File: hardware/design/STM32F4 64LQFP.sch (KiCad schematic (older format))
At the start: 17 parts, among them U1 STM32F40X_LQFP64, X2 8MHz 10ppm

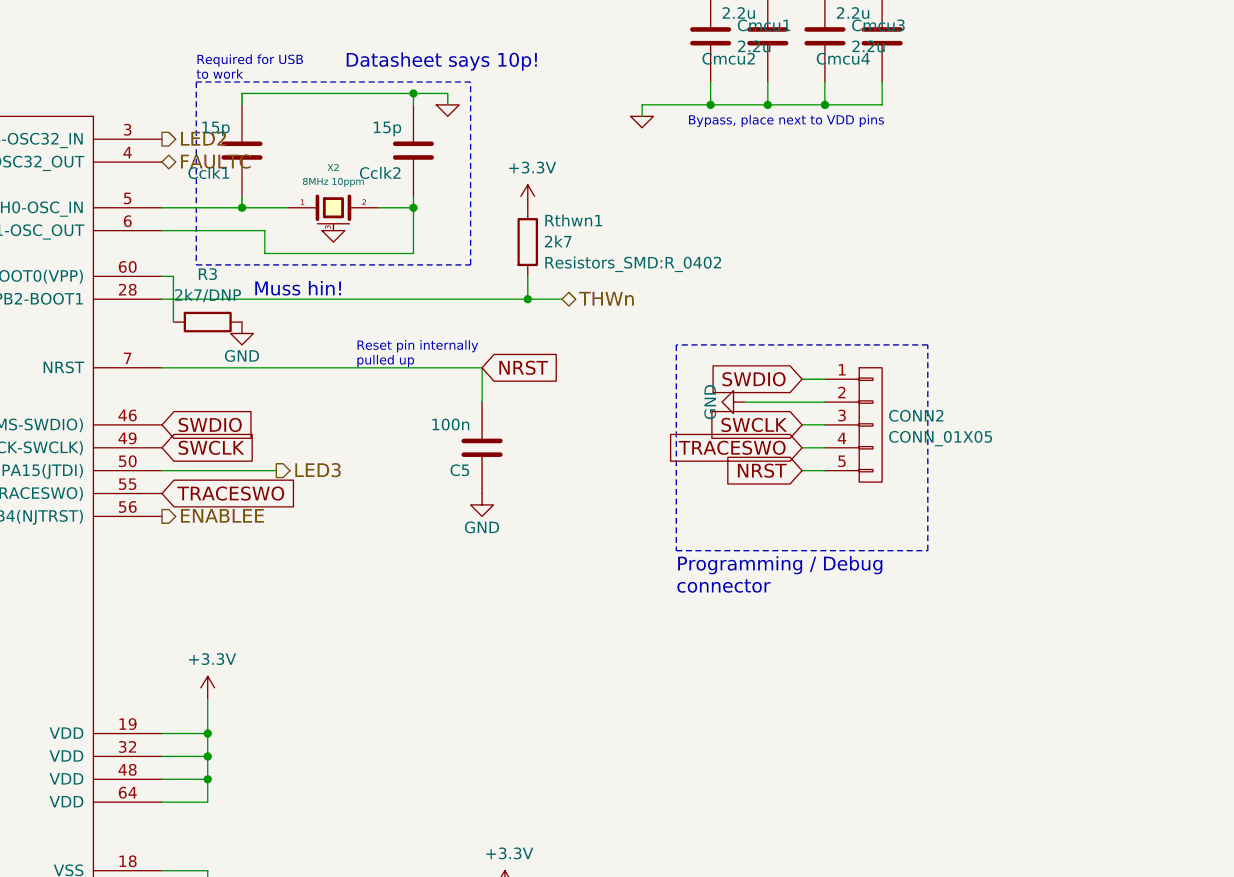
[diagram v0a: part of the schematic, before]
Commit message: Added pads for emergency bootloader execution.
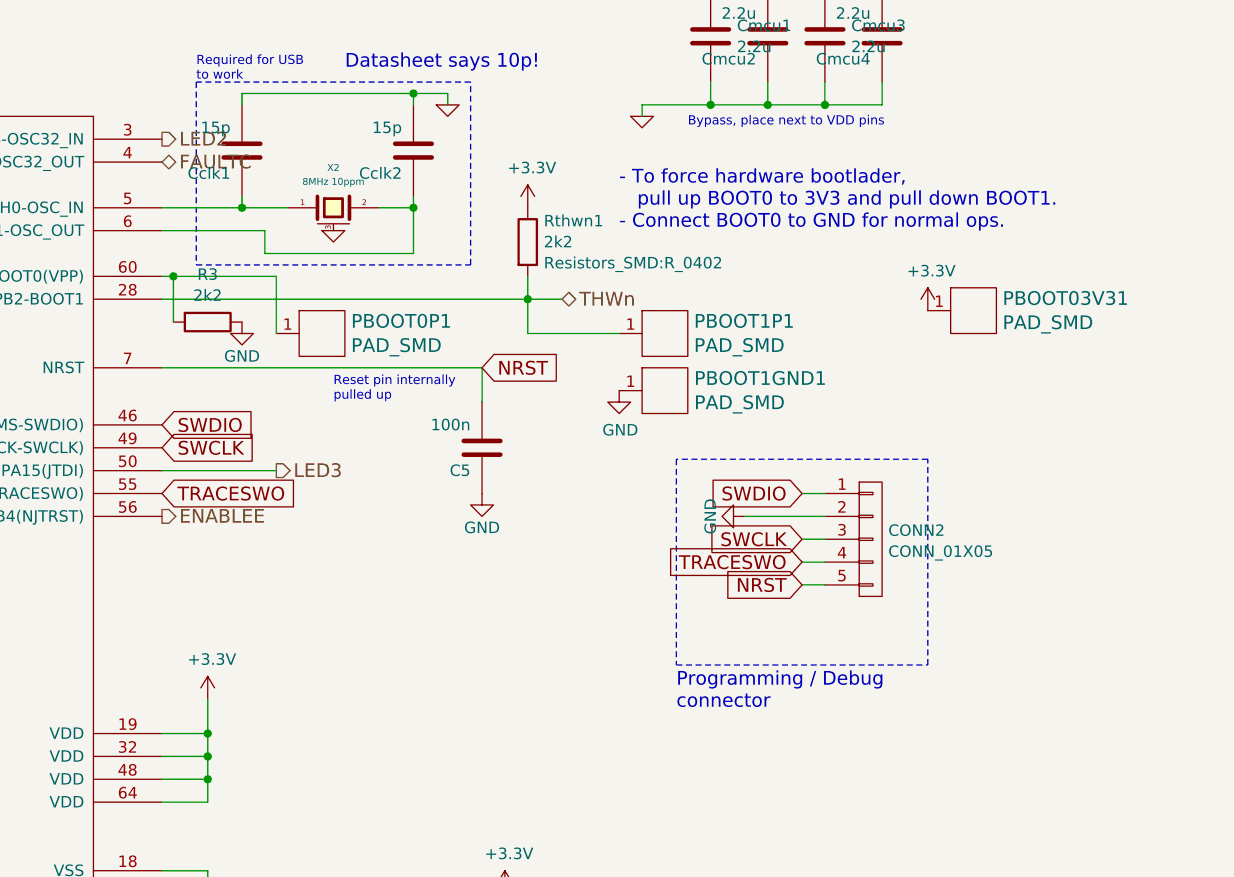
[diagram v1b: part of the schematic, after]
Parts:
- added PBOOT03V31, PBOOT0P1, PBOOT1GND1, PBOOT1P1: PAD_SMD, Pads:PAD_SMD_1x1, symbol PAD_SMD
- R3: value 2k7/DNP -> 2k2
- Rthwn1: value 2k7 -> 2k2
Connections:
- net +3V3: now also PBOOT03V31.1 (PAD)
- net GND: now also PBOOT1GND1.1 (PAD)
- net THWn: now also PBOOT1P1.1 (PAD)
- net at R3.2, U1.60 (BOOT0(VPP)): now also PBOOT0P1.1 (PAD)
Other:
- note added: "- To force hardware bootlader,\n pull up BOOT0 to 3V3 and pull down BOOT1.\n- Connect BOOT0 to GND for normal ops."
- note removed: "Muss hin!"
- moved on the sheet: CONN2
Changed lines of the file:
@@
 	-1   0    0    1
 $EndComp
-Text GLabel 9800 3000 0    60   Input ~ 0
+Text GLabel 9800 3500 0    60   Input ~ 0
 SWCLK
-Text GLabel 9800 2800 0    60   Input ~ 0
+Text GLabel 9800 3300 0    60   Input ~ 0
 SWDIO
-Text GLabel 9800 3200 0    60   Input ~ 0
+Text GLabel 9800 3700 0    60   Input ~ 0
 NRST
 $Comp
@@
 AN_IN
 Wire Notes Line
-	9250 2650 9250 3550
+	9250 3150 9250 4050
 Wire Notes Line
-	9250 3550 10350 3550
+	9250 4050 10350 4050
 Wire Notes Line
-	10350 3550 10350 2650
+	10350 4050 10350 3150
 Wire Notes Line
-	10350 2650 9250 2650
-Text Notes 9250 3750 0    60   ~ 0
+	10350 3150 9250 3150
+Text Notes 9250 4250 0    60   ~ 0
 Programming / Debug\nconnector
 Wire Wire Line
@@
 Wire Wire Line
 	8400 2750 8400 2900
-Text Notes 7850 2750 0    40   ~ 0
+Text Notes 7750 2900 0    40   ~ 0
 Reset pin internally\npulled up
 Text GLabel 8400 2750 2    60   Input ~ 0
@@
 L GND #PWR0109
 U 1 1 55E72286
-P 9550 2900
-F 0 "#PWR0109" H 9550 2650 50  0001 C CNN
-F 1 "GND" H 9550 2750 50  0000 C CNN
-F 2 "" H 9550 2900 60  0000 C CNN
-F 3 "" H 9550 2900 60  0000 C CNN
-	1    9550 2900
+P 9550 3400
+F 0 "#PWR0109" H 9550 3150 50  0001 C CNN
+F 1 "GND" H 9550 3250 50  0000 C CNN
+F 2 "" H 9550 3400 60  0000 C CNN
+F 3 "" H 9550 3400 60  0000 C CNN
+	1    9550 3400
 	0    1    1    0
 $EndComp
@@
 	1    0    0    -1
 $EndComp
-Text GLabel 9800 3100 0    60   Input ~ 0
+Text GLabel 9800 3600 0    60   Input ~ 0
 TRACESWO
 Text GLabel 7000 3300 2    60   Input ~ 0
@@
 L CONN_01X05 CONN2
 U 1 1 56A6A68D
-P 10100 3000
-F 0 "CONN2" H 10177 3038 50  0000 L CNN
-F 1 "CONN_01X05" H 10177 2946 50  0000 L CNN
-F 2 "Pads:Pin_Header_Straight_1x05_Pitch1.27mm" H 10100 3000 50  0001 C CNN
-F 3 "" H 10100 3000 50  0000 C CNN
-	1    10100 3000
+P 10100 3500
+F 0 "CONN2" H 10177 3538 50  0000 L CNN
+F 1 "CONN_01X05" H 10177 3446 50  0000 L CNN
+F 2 "Pads:Pin_Header_Straight_1x05_Pitch1.27mm" H 10100 3500 50  0001 C CNN
+F 3 "" H 10100 3500 50  0000 C CNN
+	1    10100 3500
 	1    0    0    -1
 $EndComp
 Wire Wire Line
-	9800 2800 9900 2800
+	9800 3300 9900 3300
 Wire Wire Line
-	9550 2900 9900 2900
+	9550 3400 9900 3400
 Wire Wire Line
-	9800 3000 9900 3000
+	9800 3500 9900 3500
 Wire Wire Line
-	9800 3100 9900 3100
+	9800 3600 9900 3600
 Wire Wire Line
-	9800 3200 9900 3200
+	9800 3700 9900 3700
 Text HLabel 4500 1850 0    60   Output ~ 0
 PWMF
@@
 P 7200 2550
 F 0 "R3" V 6992 2550 50  0000 C CNN
-F 1 "2k7/DNP" V 7084 2550 50  0000 C CNN
+F 1 "2k2" V 7084 2550 50  0000 C CNN
 F 2 "Resistors_SMD:R_0402" V 7084 2550 50  0001 C CNN
 F 3 "" H 7200 2550 50  0000 C CNN
@@
 $EndComp
 Wire Wire Line
-	7000 2350 7050 2350
+	7000 2350 7500 2350
 Wire Wire Line
 	7050 2350 7050 2550
@@
 P 8600 2200
 F 0 "Rthwn1" H 8670 2292 50  0000 L CNN
-F 1 "2k7" H 8670 2200 50  0000 L CNN
+F 1 "2k2" H 8670 2200 50  0000 L CNN
 F 2 "Resistors_SMD:R_0402" H 8670 2108 50  0000 L CNN
 F 3 "" H 8600 2200 50  0000 C CNN
@@
 $EndComp
 Wire Wire Line
-	8600 2350 8600 2450
+	8600 2350 8600 2600
 Connection ~ 8600 2450
-Text Notes 7400 2450 0    60   ~ 0
-Muss hin!
+Text Notes 9000 2150 0    60   ~ 0
+- To force hardware bootlader,\n   pull up BOOT0 to 3V3 and pull down BOOT1.\n- Connect BOOT0 to GND for normal ops.
+$Comp
+L PAD_SMD PBOOT1P1
+U 1 1 579EE0ED
+P 9200 2600
+F 0 "PBOOT1P1" H 9327 2653 60  0000 L CNN
+F 1 "PAD_SMD" H 9327 2547 60  0000 L CNN
+F 2 "Pads:PAD_SMD_1x1" H 9200 2350 60  0001 C CNN
+F 3 "" H 9200 2450 60  0000 C CNN
+	1    9200 2600
+	1    0    0    -1
+$EndComp
+Wire Wire Line
+	8600 2600 9000 2600
+$Comp
+L GND #PWR0117
+U 1 1 579EE6A9
+P 9000 2850
+F 0 "#PWR0117" H 9000 2600 50  0001 C CNN
+F 1 "GND" H 9005 2677 50  0000 C CNN
+F 2 "" H 9000 2850 50  0000 C CNN
+F 3 "" H 9000 2850 50  0000 C CNN
+	1    9000 2850
+	1    0    0    -1
+$EndComp
+$Comp
+L PAD_SMD PBOOT1GND1
+U 1 1 579EE6E1
+P 9200 2850
+F 0 "PBOOT1GND1" H 9328 2903 60  0000 L CNN
+F 1 "PAD_SMD" H 9328 2797 60  0000 L CNN
+F 2 "Pads:PAD_SMD_1x1" H 9200 2600 60  0001 C CNN
+F 3 "" H 9200 2700 60  0000 C CNN
+	1    9200 2850
+	1    0    0    -1
+$EndComp
+$Comp
+L PAD_SMD PBOOT0P1
+U 1 1 579EE936
+P 7700 2600
+F 0 "PBOOT0P1" H 7827 2653 60  0000 L CNN
+F 1 "PAD_SMD" H 7827 2547 60  0000 L CNN
+F 2 "Pads:PAD_SMD_1x1" H 7700 2350 60  0001 C CNN
+F 3 "" H 7700 2450 60  0000 C CNN
+	1    7700 2600
+	1    0    0    -1
+$EndComp
+Wire Wire Line
+	7500 2350 7500 2600
+Connection ~ 7050 2350
+$Comp
+L PAD_SMD PBOOT03V31
+U 1 1 579EF824
+P 10550 2500
+F 0 "PBOOT03V31" H 10677 2553 60  0000 L CNN
+F 1 "PAD_SMD" H 10677 2447 60  0000 L CNN
+F 2 "Pads:PAD_SMD_1x1" H 10550 2250 60  0001 C CNN
+F 3 "" H 10550 2350 60  0000 C CNN
+	1    10550 2500
+	1    0    0    -1
+$EndComp
+$Comp
+L +3.3V #PWR0118
+U 1 1 579EFAF8
+P 10350 2500
+F 0 "#PWR0118" H 10350 2350 50  0001 C CNN
+F 1 "+3.3V" H 10365 2673 50  0000 C CNN
+F 2 "" H 10350 2500 50  0000 C CNN
+F 3 "" H 10350 2500 50  0000 C CNN
+	1    10350 2500
+	1    0    0    -1
+$EndComp
 $EndSCHEMATC

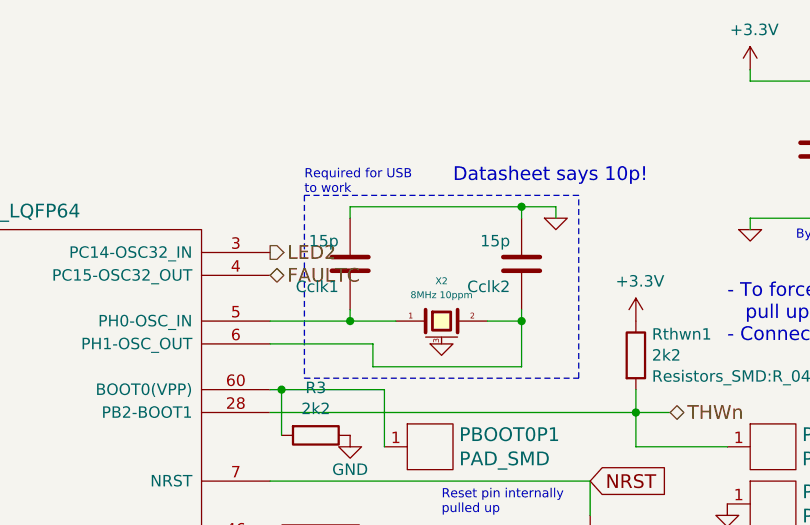
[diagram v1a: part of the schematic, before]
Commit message: TODO Double-check BOM. Check silk screen. Check Gerber output.
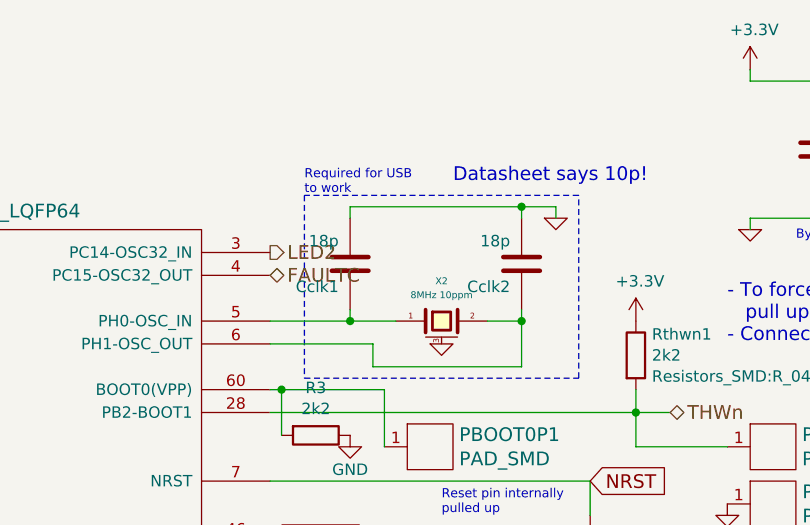
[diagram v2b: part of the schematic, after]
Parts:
- Cclk1, Cclk2: value 15p -> 18p; Comment (none) -> for the crystal
- X2: Part Number (none) -> ABM3B-8.0-10-1UT; mfg# ABM3B-8.0-10-1UT -> (none)
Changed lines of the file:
@@
 P 7350 1800
 F 0 "Cclk1" H 7400 1900 50  0000 L CNN
-F 1 "15p" H 7400 1700 50  0000 L CNN
+F 1 "18p" H 7400 1700 50  0000 L CNN
 F 2 "Capacitors_SMD:C_0402" H 7350 1800 60  0001 C CNN
 F 3 "" H 7350 1800 60  0001 C CNN
+F 4 "for the crystal" H 7350 1800 60  0001 C CNN "Comment"
 	1    7350 1800
 	-1   0    0    1
@@
 P 8100 1800
 F 0 "Cclk2" H 8150 1900 50  0000 L CNN
-F 1 "15p" H 8150 1700 50  0000 L CNN
+F 1 "18p" H 8150 1700 50  0000 L CNN
 F 2 "Capacitors_SMD:C_0402" H 8100 1800 60  0001 C CNN
 F 3 "" H 8100 1800 60  0001 C CNN
+F 4 "for the crystal" H 8100 1800 60  0001 C CNN "Comment"
 	1    8100 1800
 	-1   0    0    1
@@
 F 2 "Crystals_User:Crystal_5x3mm" H 7750 2050 60  0001 C CNN
 F 3 "" H 7750 2050 60  0000 C CNN
-F 4 "ABM3B-8.0-10-1UT" H 7750 2050 60  0001 C CNN "mfg#"
+F 4 "ABM3B-8.0-10-1UT" H 7750 2050 60  0001 C CNN "Part Number"
 	1    7750 2050
 	1    0    0    -1

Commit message: Swapped STM32 Pin33 and Pin50 and added some pads to enable usage of USART3 when TIM8 is bridged to PWM d,e,f.
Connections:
- net LED3: now also U1.33 (PB12); no longer U1.50 (PA15(JTDI))
- net ZCD_EN: now also U1.50 (PA15(JTDI)); no longer U1.33 (PB12)
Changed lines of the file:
@@
 Text HLabel 7000 1850 2    60   3State ~ 0
 FAULTC
-Text HLabel 4500 4050 0    60   Output ~ 0
+Text HLabel 7500 3200 2    60   Output ~ 0
 ZCD_EN
 $Comp
@@
 Text HLabel 7000 1750 2    60   Output ~ 0
 LED2
-Text HLabel 7500 3200 2    60   Output ~ 0
+Text HLabel 4500 4050 0    60   Output ~ 0
 LED3
 Text HLabel 4500 6050 0    60   Output ~ 0

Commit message: Prepare for fab.
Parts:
- X2: symbol CRYSTAL_SMD -> CRYSTAL_SMD-RESCUE-DrChibi
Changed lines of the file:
@@
 EESchema Schematic File Version 2
+LIBS:DrChibi-rescue
 LIBS:BLDC_4-rescue
 LIBS:power
@@
 encoding utf-8
 Sheet 11 11
-Title "3-Phase Universal Driver"
-Date "2015-08-27"
-Rev "0.1"
+Title "DrChibi, Looong-Strip"
+Date "2016-10-24"
+Rev "1"
 Comp "Jörg Wangemann"
-Comment1 ""
+Comment1 "Microcontroller STM32"
 Comment2 ""
 Comment3 "CC-BY-SA 4.0"
@@
 SENSCE
 $Comp
-L CRYSTAL_SMD X2
+L CRYSTAL_SMD-RESCUE-DrChibi X2
 U 1 1 540978A3
 P 7750 2050
+AR Path="/540978A3" Ref="X2"  Part="1"
+AR Path="/53F7501A/540978A3" Ref="X2"  Part="1"
 F 0 "X2" H 7750 2225 30  0000 C CNN
 F 1 "8MHz 10ppm" H 7750 2164 30  0000 C CNN
